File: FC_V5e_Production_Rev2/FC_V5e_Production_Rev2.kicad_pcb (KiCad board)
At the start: 4 copper layers, 88 x 94.5 mm, 259 parts, among them IC3 RV-3028-C7_32.768kHz_1ppm_TA_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, IC6 LT3652IMSE#PBF, J1 Conn_01x06, J10 INHIBIT_P2, J11 Conn_01x06, J12 USB_C_Receptacle_USB2.0_16P, J13 Conn_01x06, J14 Battery Input, J15 ISS_INHIBIT_Picolock, J16 DEBUG, J18 Payload, J19 ISS_INHIBIT, J2 Conn_01x06, J20 RBF_Inhibit, J21 Heater Output, J22 SWD Port, J23 Aux Deploy 1, J24 Deploy 2, J29 INHIBIT_S2_Picolock, J3 Life Makes Lemonade, J30 RBF_Picolock, J4 Conn_01x02, J5 BM04B-SRSS-TB(LF)(SN), J6 Conn_01x06, J7 INHIBIT_P1, J8 INHIBIT_S1_Picolock, J9 Conn_01x06, SW1 KMR2, SW2 KMR2, U1 TLV1704, U10 TPS54226PWPRPWP14_2P31X2P46-L, U11 W25Q128JVS, U12 LT8610ABEMSE#TRPBF, U13 E22-400M30S, U15 LIS2MDL, U16 INA219AxDCN, U18 RP2350_60QFN, U19 AP22653AW6-7, U2 ZDSD04GLGEAG, U21 AP22653AW6-7, U22 AP22653AW6-7, U23 AP22653AW6-7, U24 AP22653AW6-7, U25 TPS2HB50AQPWPRQ1, U27 AP22653AW6-7, U29 AP22653AW6-7, U3 TCA9548APWR, U30 E28-2G4M27S, U6 TPS4H160AQPWPRQ1, U7 LSM6DSOTR, U8 INA219AxDCN, U9 MCP23017_SS, Y1 ABM8-272-T3

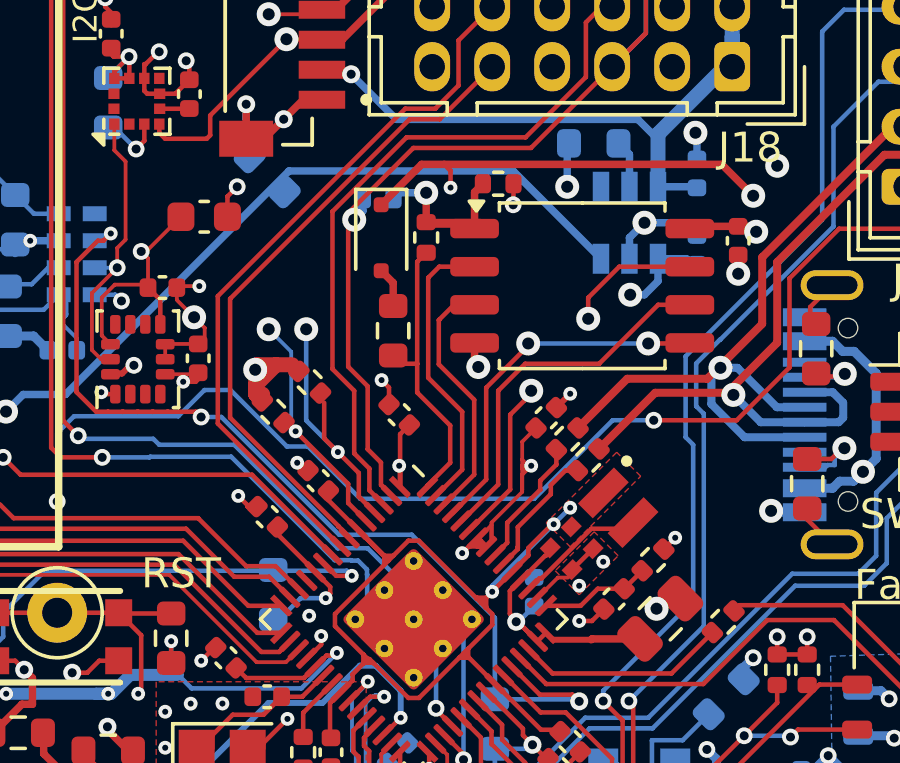
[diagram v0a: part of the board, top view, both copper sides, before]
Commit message: V5e_Rev2: Restore APS1604M PSRAM in layout
Transplants U5, C10 and R37 footprints plus the PSRAM_CS/QSPI tracks and
local GND/+3V3 stubs from the pre-removal V5e layout back to their
original positions (U5 on B.Cu under the flash). Zones refilled.

Two items were left out to avoid disturbing Rev1 copper:
- A GND via at (202.04, 80.06) that Rev1 had nudged to (202.2, 80.2);
  re-adding it would duplicate the via.
- The QSPI_SCLK B.Cu run along y=71.82 between (207.5, 71.8) and
  (211.8, 73.8), which now collides with a +3V3 via Rev1 added at
  (209.4, 71.6). SCLK is therefore intentionally left with one
  unconnected gap pending a decision on how to route around that via.

DRC vs the pre-change board: no new violations other than the
deliberate SCLK gap (1 unconnected, 2 dangling-track warnings).
Schematic parity: clean.

Co-Authored-By: Claude Fable 5.1 <noreply@anthropic.com>
Claude-Session: https://claude.ai/code/session_01DCKHZ2rqY43d2eGoEeJM1Y
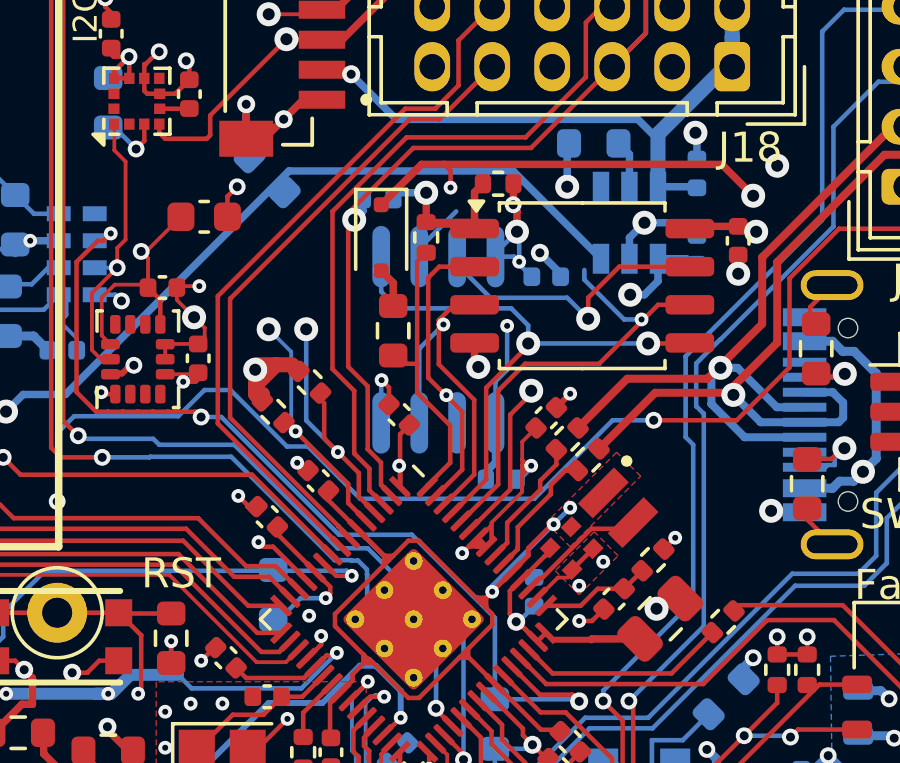
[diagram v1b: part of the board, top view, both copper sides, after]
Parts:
- added C10: 100n, Capacitor_SMD:C_0402_1005Metric, B.Cu at (210.5, 74.0)
- added R37: 10k, Resistor_SMD:R_0402_1005Metric, B.Cu at (209.0, 80.8)
- added U5: APS1604M-3SQR-SN_C18214056, FC_DEV_BOARD:SOIC-8_L4.9-W3.9-P1.27-LS6.0-BL, B.Cu at (206.9, 76.1)
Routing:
- net /RP2350AHHHHHHHHH/PSRAM_CS: track 0.00 -> 19.2 mm, vias 0 -> 2
- net /RP2350AHHHHHHHHH/QSPI_SD0: track 12.1 -> 19.2 mm
- net +3V3: track 206.3 -> 212.3 mm, vias 60 -> 62
- net /RP2350AHHHHHHHHH/QSPI_SD3: track 13.2 -> 18.6 mm
- net /RP2350AHHHHHHHHH/QSPI_SCLK: track 12.5 -> 17.3 mm, vias 0 -> 1
- net /RP2350AHHHHHHHHH/QSPI_SD2: track 7.81 -> 11.6 mm, vias 0 -> 1
- net GND: track 263.5 -> 266.4 mm, vias 174 -> 175
- net /RP2350AHHHHHHHHH/QSPI_SD1: track 9.83 -> 10.9 mm, vias 0 -> 1
